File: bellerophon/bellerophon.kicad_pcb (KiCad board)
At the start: 2 copper layers, 55 x 143 mm, 24 parts, among them IC1 L7805ACV, IC2 Adafruit_MPL3115A2, Q1 IRLB8721PBF, Q2 IRLB8721PBF, U1 Adafruit_ICM20948, U2 Teensy4.0, U3 Adafruit SPI Flash SD Card

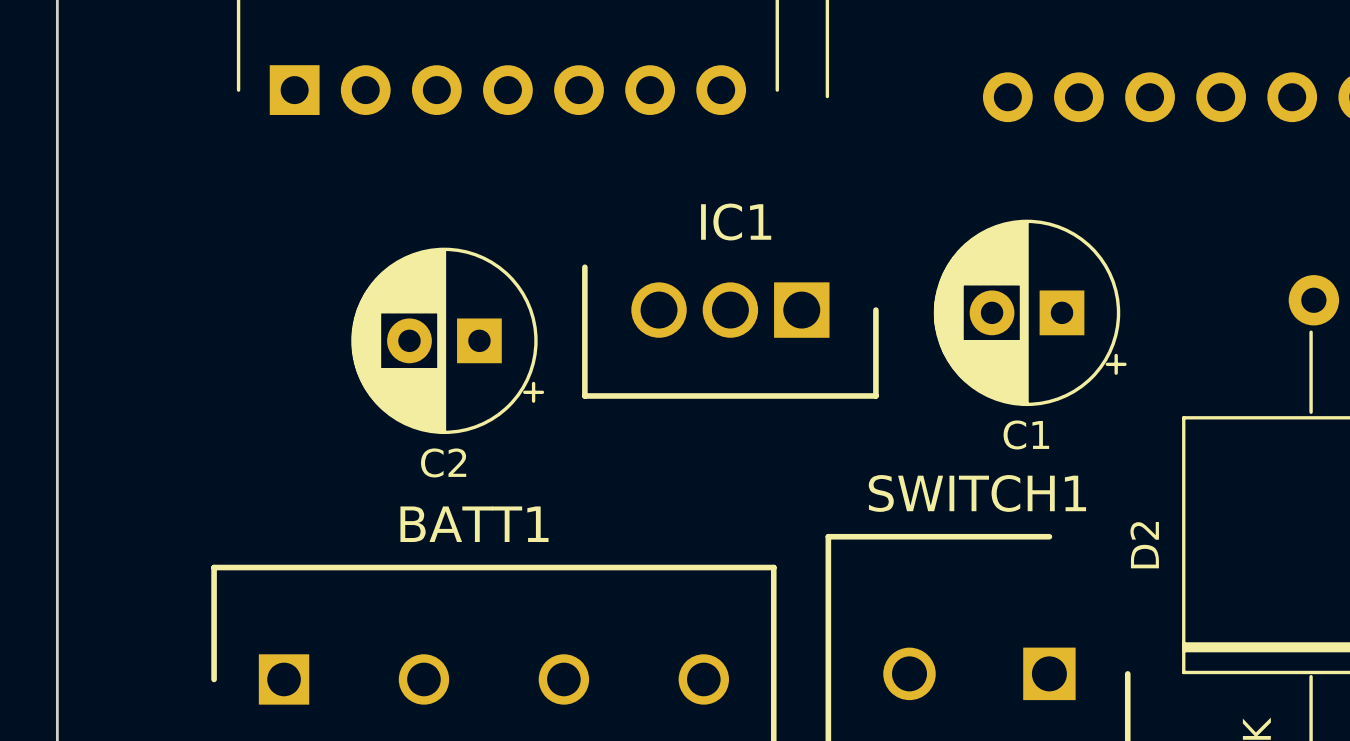
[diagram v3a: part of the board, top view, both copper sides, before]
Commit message: change capacitor footprint to D10mm
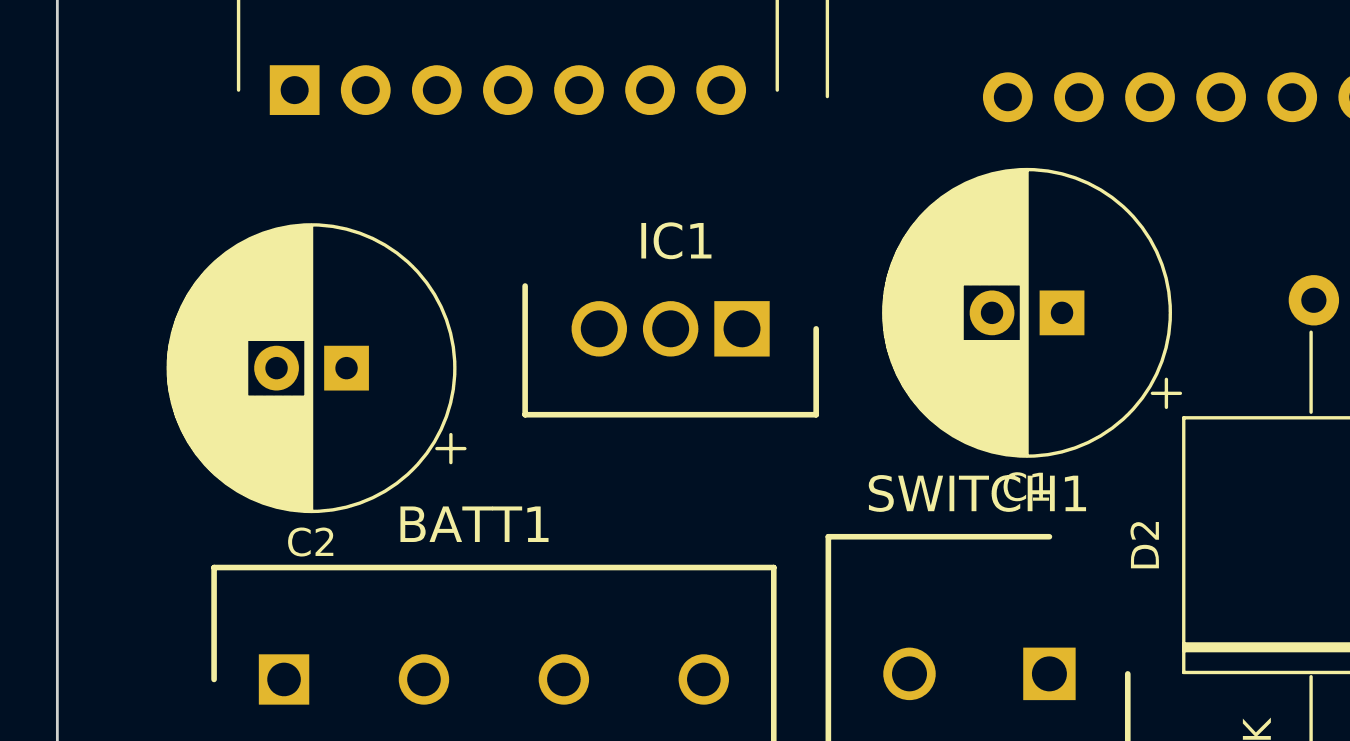
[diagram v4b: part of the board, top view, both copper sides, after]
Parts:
- C1, C2: footprint Capacitor_THT:CP_Radial_D6.3mm_P2.50mm -> Capacitor_THT:CP_Radial_D10.0mm_P2.50mm
- moved C2 4.85 mm to (70.3, 142.9)
- moved IC1 2.24 mm to (84.5, 141.5)

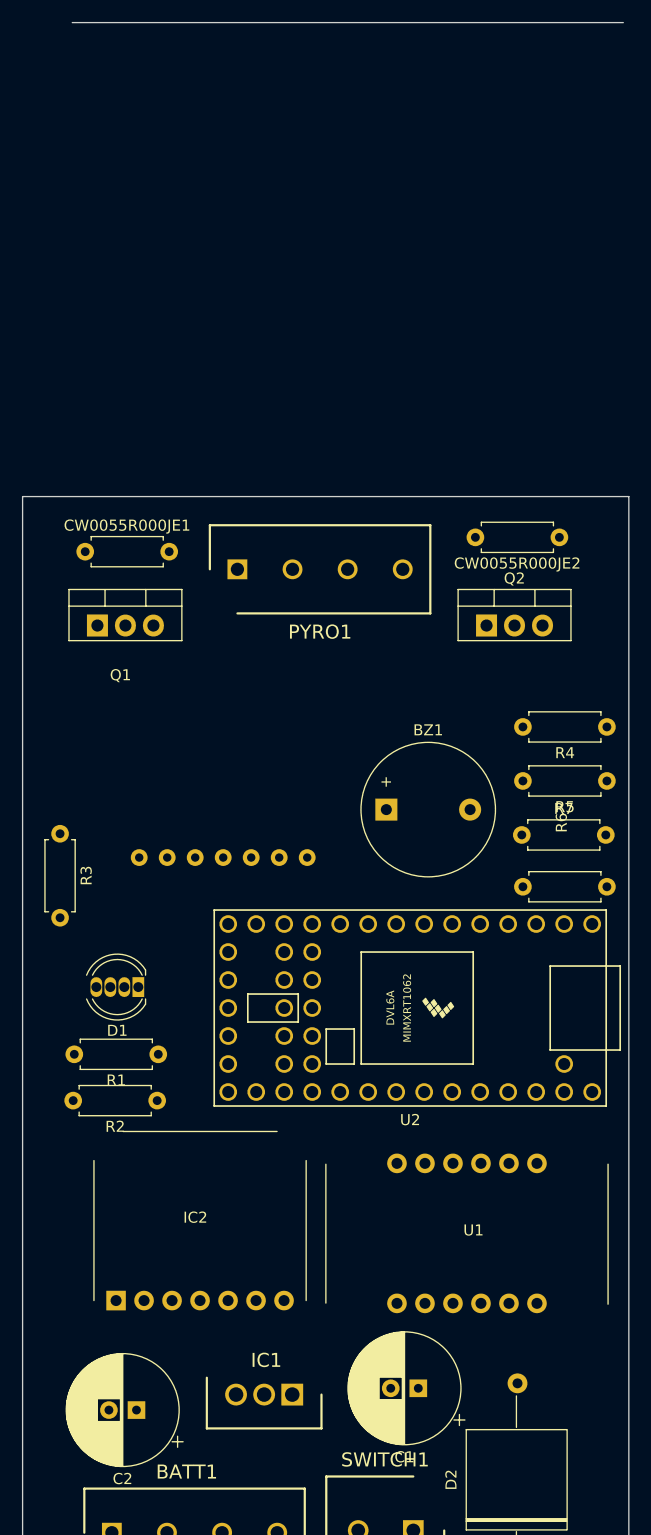
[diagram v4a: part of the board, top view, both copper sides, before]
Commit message: add second buzzer
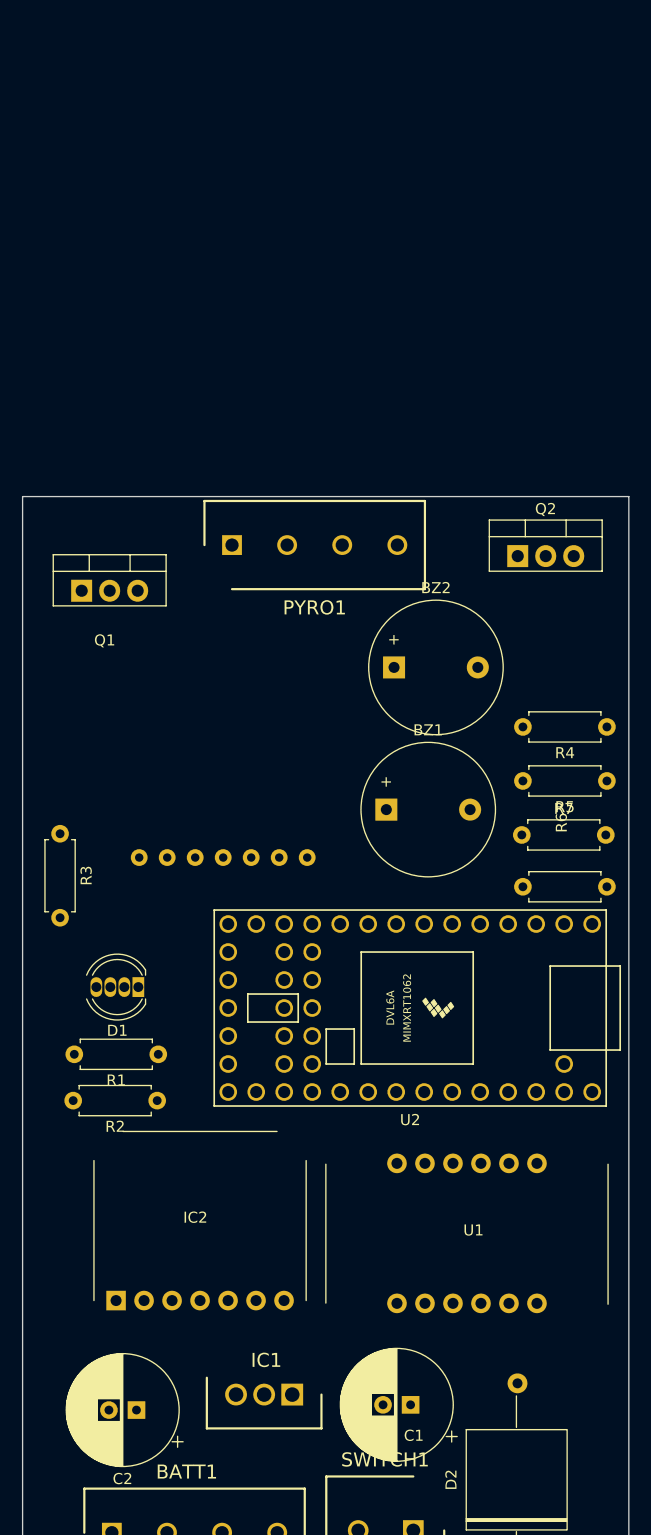
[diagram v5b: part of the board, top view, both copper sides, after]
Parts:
- removed CW0055R000JE1, CW0055R000JE2: 5 ohms, Resistor_THT:R_Axial_DIN0207_L6.3mm_D2.5mm_P7.62mm_Horizontal
- added BZ2: Buzzer, Buzzer:PiezoBuzzer-PS1240, F.Cu at (93.7, 75.5)
- moved Q2 6.91 mm to (104.9, 65.4)
- moved Q1 3.46 mm to (65.4, 68.5)
- moved PYRO1 2.25 mm to (79.0, 64.4)
- moved C1 1.66 mm to (95.2, 142.4)
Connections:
- net BZR renamed BZR1
- PYRO1 pad 1: Net-(CW0055R000JE1-Pad2) -> Net-(PYRO1-Pad1)
- PYRO1 pad 4: Net-(CW0055R000JE2-Pad2) -> Net-(PYRO1-Pad4)
- Q1 pad 2: Net-(CW0055R000JE1-Pad1) -> Net-(PYRO1-Pad1)
- Q2 pad 2: Net-(CW0055R000JE2-Pad1) -> Net-(PYRO1-Pad4)
- U2 pad 8: unconnected-(U2-Pad8) -> BZR2
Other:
- board size 55 x 143 mm -> 55 x 100 mm

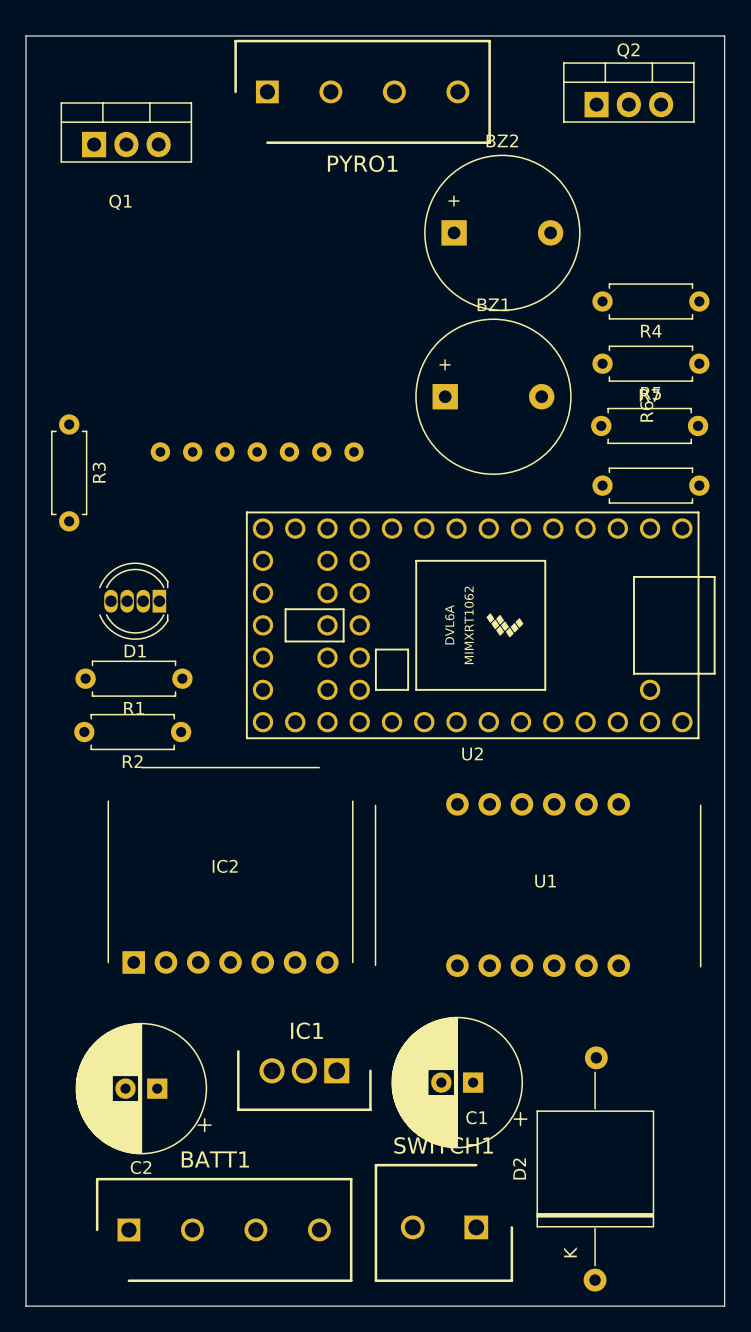
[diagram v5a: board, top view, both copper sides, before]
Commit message: add mounting holes, refined component placement
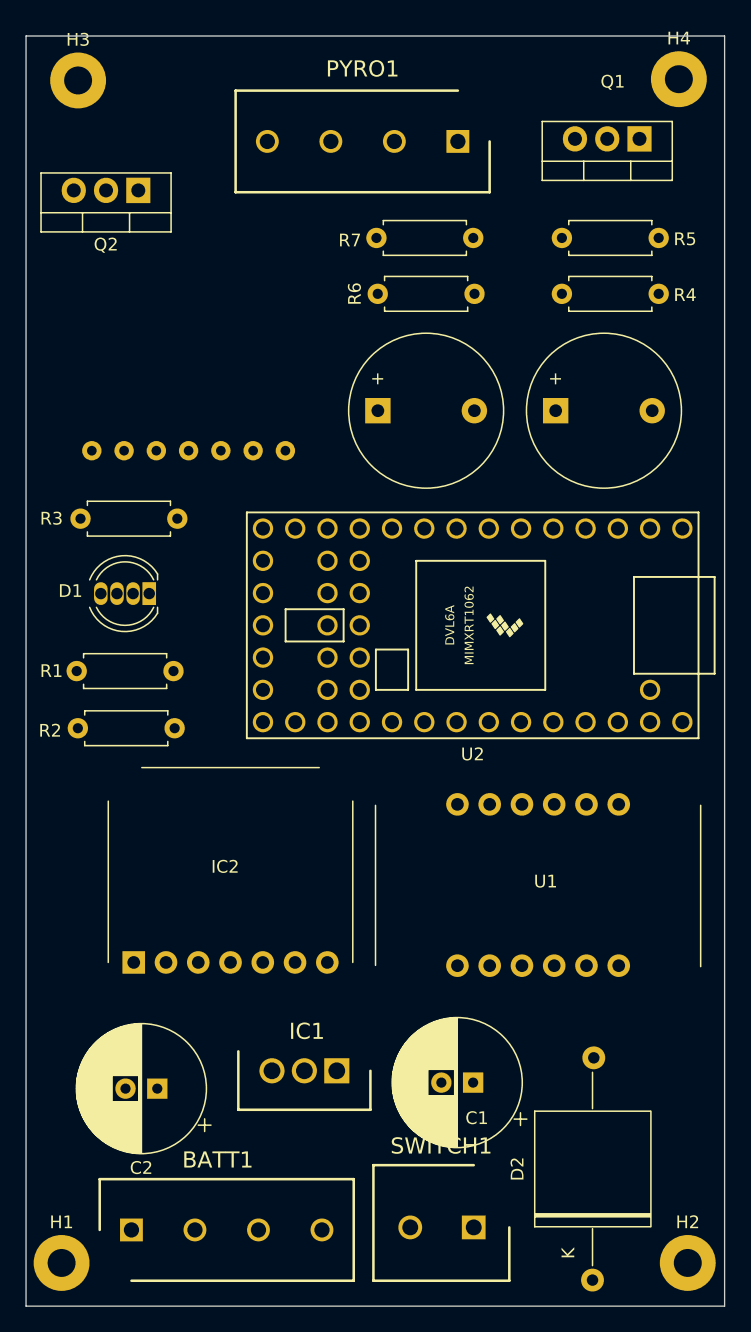
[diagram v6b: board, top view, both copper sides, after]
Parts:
- added H1: MountingHole_Pad, MountingHole:MountingHole_2.2mm_M2_Pad, F.Cu at (62.8, 156.6)
- added H2: MountingHole_Pad, MountingHole:MountingHole_2.2mm_M2_Pad, F.Cu at (112.1, 156.6)
- added H3: MountingHole_Pad, MountingHole:MountingHole_2.2mm_M2_Pad, F.Cu at (64.1, 63.5)
- added H4: MountingHole_Pad, MountingHole:MountingHole_2.2mm_M2_Pad, F.Cu at (111.4, 63.4)
- moved Q1 42.9 mm to (108.3, 68.1), turned to 180 degrees
- moved Q2 36.7 mm to (68.8, 72.2), turned to 180 degrees
- moved R6 29.5 mm to (87.7, 80.3), turned to 0 degrees
- moved R7 17.9 mm to (95.2, 75.9), turned to 180 degrees
- moved BZ2 16.1 mm to (101.7, 89.5)
- moved PYRO1 15.5 mm to (94.0, 68.3), turned to 180 degrees
- moved R5 14.7 mm to (102.2, 75.9), turned to 0 degrees
- moved R3 11.3 mm to (71.9, 98.0), turned to 180 degrees
- moved BZ1 5.41 mm to (87.7, 89.5)
- moved U3 5.40 mm to (72.8, 86.3)
- moved R4 3.26 mm to (109.8, 80.3)
- moved D1 1.00 mm to (69.7, 103.9)
- moved R1 0.92 mm to (71.6, 110.0)
- moved R2 0.59 mm to (71.7, 114.5)
- moved BATT1 0.20 mm to (68.3, 154.0)
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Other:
- rule pad_to_mask_clearance: 0 -> 0.05
